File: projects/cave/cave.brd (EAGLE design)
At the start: 160 x 100 mm, 115 parts, among them U1 IRLML6344TRPBF, U10 IRLML6344TRPBF, U11 IRLML6344TRPBF, U12 IRLML6344TRPBF, U2 TLC555CDR, U3 IRLML6344TRPBF, U4 IRLML6344TRPBF, U5 IRLML6344TRPBF, U6 IRLML6344TRPBF, U7 TPS54625, U9 IRLML6344TRPBF

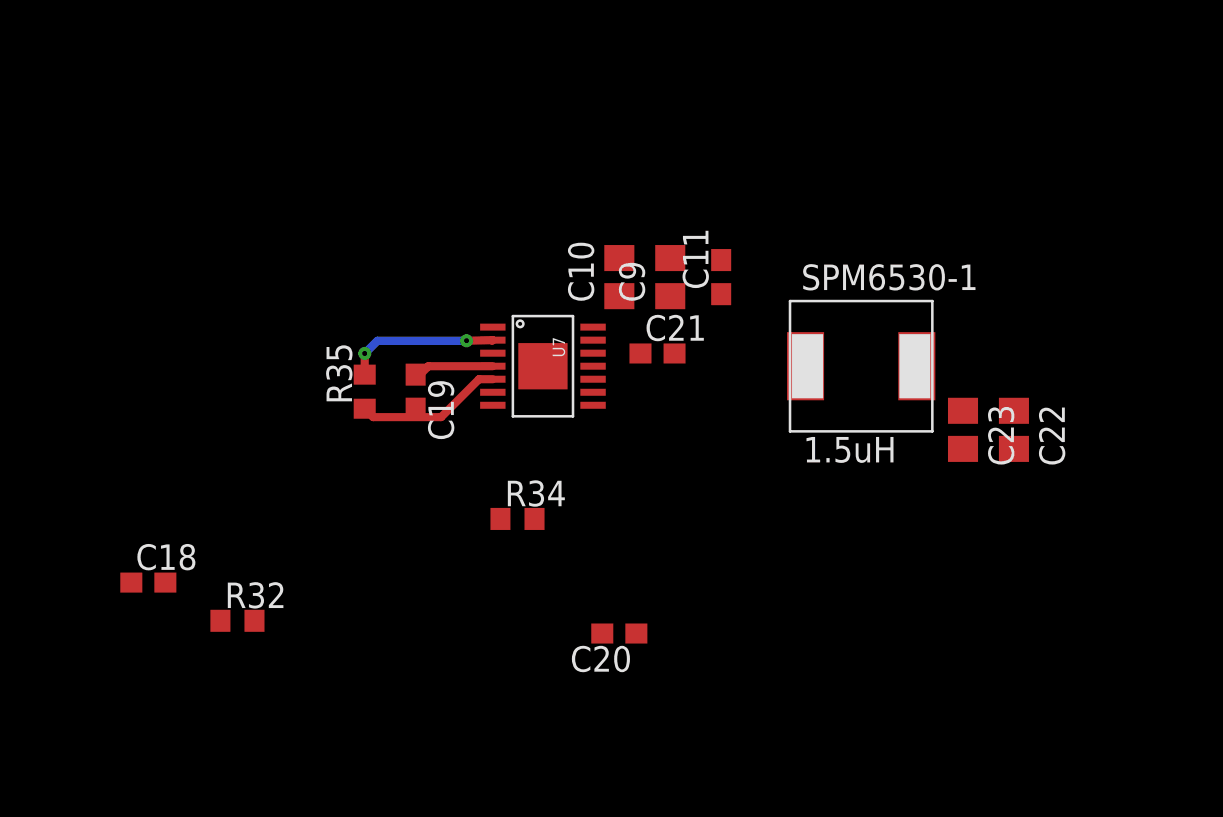
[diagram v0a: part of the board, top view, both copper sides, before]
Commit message: 5V step down regulator routed
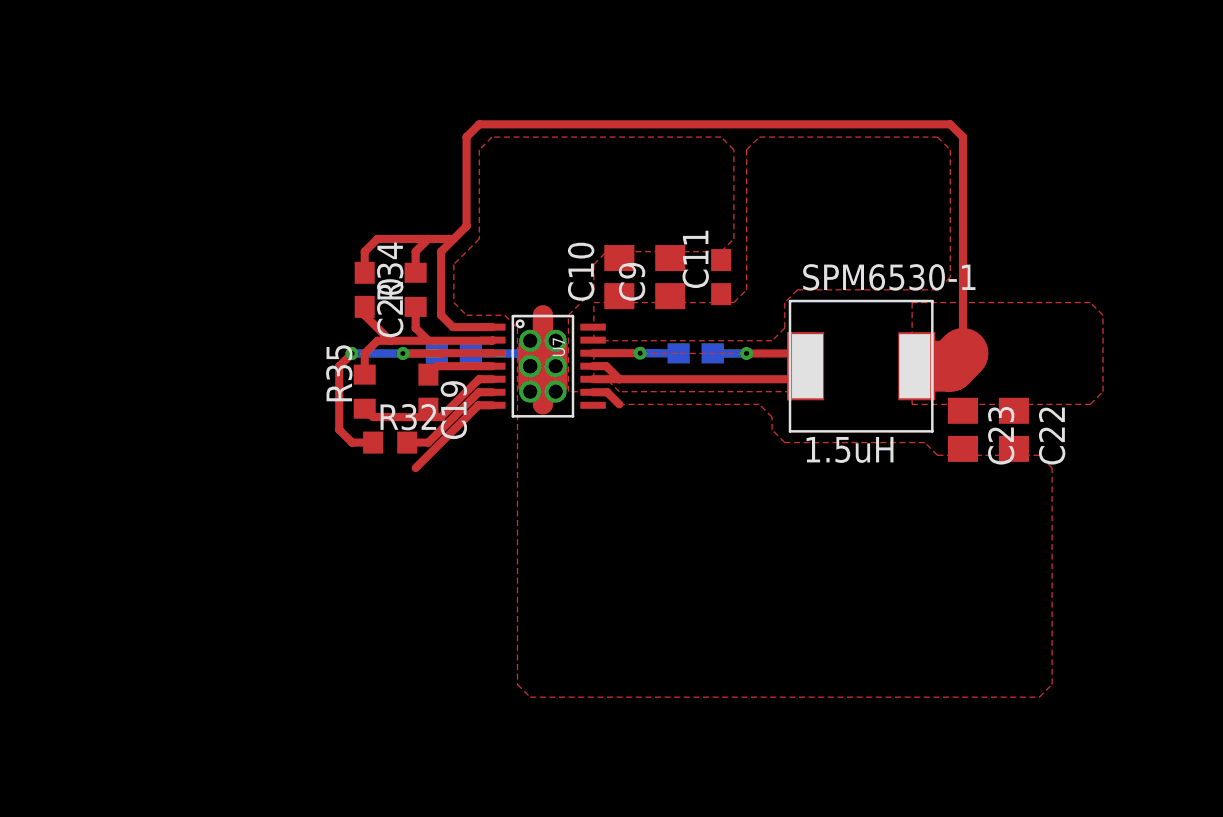
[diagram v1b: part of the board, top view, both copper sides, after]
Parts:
- moved C20 21.3 mm to (92.1, 33.7), turned to 270 degrees
- moved C18 19.0 mm to (96.5, 30.5), flipped to the bottom, turned to 180 degrees
- moved R34 12.5 mm to (94.6, 33.7), turned to 90 degrees
- moved R32 11.7 mm to (93.3, 26.0)
- moved C21 1.90 mm to (108.6, 30.5), flipped to the bottom, turned to 180 degrees
- moved C19 0.64 mm to (95.2, 28.6)
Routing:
- net +5V: track 0.00 -> 58.2 mm
- net N$36: track 0.00 -> 16.0 mm, vias 0 -> 1
- net N$28: track 0.00 -> 14.7 mm, vias 0 -> 2
- net GND: track 7.35 -> 17.8 mm, vias 0 -> 1
- net N$30: track 0.00 -> 5.31 mm
- net ENABLE: track 0.00 -> 5.15 mm
- net N$35: track 0.00 -> 4.27 mm, vias 0 -> 1
- net N$34: track 7.75 -> 11.9 mm, vias 2 -> 0
- net N$31: track 4.02 -> 3.39 mm
- net VCOND: track 0.00 -> 0.59 mm
- added copper zone on layer 1, net +5V
- added copper zone on layer 1, net GND
- added copper zone on layer 1, net N$36
- added copper zone on layer 1, net VCOND

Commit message: finished routing 5V step down regulator
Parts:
- X2: device con-subd:F09H -> con-subd:F09V
- moved C3 295.5 mm to (101.0, 19.1), turned to 90 degrees
- moved SMW5-2 246.8 mm to (39.4, 26.0)
- moved C2 246.4 mm to (78.1, 14.0), turned to 270 degrees
- moved SMW5-1 245.3 mm to (39.4, 34.3)
- moved C12 198.2 mm to (55.2, 19.1), turned to 90 degrees
- moved R2 104.3 mm to (27.3, 24.8), turned to 90 degrees
- moved D3 94.4 mm to (39.4, 40.6), turned to 270 degrees
- moved R3 85.4 mm to (27.3, 20.3), turned to 90 degrees
- moved T3 82.1 mm to (93.3, 33.7)
- moved R19 82.0 mm to (85.1, 33.0)
- moved R17 80.4 mm to (104.1, 34.3)
- moved U2 78.8 mm to (89.5, 40.0)
- moved D1 61.9 mm to (27.3, 30.5), turned to 270 degrees
- moved D2 36.6 mm to (52.1, 30.5), turned to 270 degrees
- moved D4 29.9 mm to (36.8, 15.9)
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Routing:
- net GND: track 17.8 -> 66.9 mm, vias 1 -> 2
- net VCOND: track 0.59 -> 12.7 mm
- net +5V: track 58.2 -> 66.8 mm
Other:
- board size 160 x 100 mm -> 227.3 x 162.7 mm

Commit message: 555 components placed but not routed. Updated 555 pin description in package.
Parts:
- moved R18 232.5 mm to (110.5, 3.81)
- moved T1 210.7 mm to (111.1, 6.99), turned to 90 degrees
- moved R7 210.3 mm to (123.2, 10.8), turned to 90 degrees
- moved C6 209.8 mm to (122.6, 6.99), turned to 270 degrees
- moved R8 209.5 mm to (114.6, 6.35), turned to 90 degrees
- moved C5 203.3 mm to (125.7, 6.35), turned to 270 degrees
- moved R6 203.3 mm to (123.2, 14.0), turned to 90 degrees
- moved T2 131.8 mm to (105.7, 4.76), turned to 180 degrees
- moved POWER- 119.0 mm to (3.17, 14.6)
- moved POWER+ 103.9 mm to (3.17, 21.0)
- moved D4 89.0 mm to (125.7, 10.8)
- moved U2 40.4 mm to (117.5, 10.8)
- moved R19 35.3 mm to (111.8, 9.84), turned to 180 degrees
- moved T3 27.1 mm to (108.0, 10.8), turned to 90 degrees
- moved R17 24.8 mm to (120.0, 15.2), turned to 270 degrees
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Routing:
- net VCOND: track 12.7 -> 148.1 mm, vias 0 -> 2
- net POWER_STATE: track 0.00 -> 35.2 mm, vias 0 -> 1
- net +12V: track 0.00 -> 28.3 mm
- net GND: track 66.9 -> 39.6 mm, vias 2 -> 1
- net N$3: track 0.00 -> 22.9 mm
- net N$2: track 0.00 -> 22.9 mm
- net N$4: track 0.00 -> 15.5 mm
- net N$6: track 0.00 -> 13.4 mm, vias 0 -> 2
- net N$1: track 0.00 -> 11.7 mm
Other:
- board size 227.3 x 162.7 mm -> 160 x 100 mm

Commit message: wip on routing
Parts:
- moved R3 7.73 mm to (15.9, 12.7)
- moved POWER+ 7.73 mm to (10.8, 19.7)
- moved POWER- 7.73 mm to (10.8, 13.3)
- moved R2 7.73 mm to (15.9, 17.1)
- moved T1 7.38 mm to (108.0, 13.7)
- moved R17 6.97 mm to (126.0, 18.7)
- moved D1 6.48 mm to (19.7, 18.4)
- moved T3 6.43 mm to (111.4, 16.2), turned to 0 degrees
- moved R18 4.80 mm to (111.1, 8.57)
- moved D2 4.55 mm to (38.1, 27.0), turned to 0 degrees
- moved T2 4.44 mm to (105.7, 9.21)
- moved D3 4.42 mm to (29.5, 28.3)
- moved SMW5-1 4.24 mm to (29.5, 22.5)
- moved SMW5-2 4.24 mm to (29.5, 14.3)
- moved R8 2.93 mm to (114.0, 9.21)
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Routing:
- net +12V: track 28.3 -> 122.7 mm
- net GND: track 39.6 -> 57.5 mm
- net ENABLE: track 5.15 -> 21.5 mm
- net VCOND: track 148.1 -> 163.1 mm, vias 2 -> 4
- net N$1: track 11.7 -> 22.3 mm
- net N$12: track 0.00 -> 9.90 mm
- net N$5: track 0.00 -> 9.33 mm
- net N$6: track 13.4 -> 21.9 mm
- net N$11: track 0.00 -> 7.39 mm
- net WATCHDOG: track 0.00 -> 6.09 mm
- net POWER_STATE: track 35.2 -> 39.9 mm
- net N$4: track 15.5 -> 11.5 mm
- net N$16: track 0.00 -> 3.47 mm
- net N$9: track 0.00 -> 2.66 mm
- net N$17: track 0.00 -> 2.25 mm

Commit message: "power" layout makeover in progress
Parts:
- moved X2 318.3 mm to (95.2, 60.6)
- moved X3 310.4 mm to (104.8, 27.0), turned to 90 degrees
- moved C21 109.7 mm to (28.3, 41.9)
- moved C22 109.7 mm to (44.1, 38.1)
- moved C23 109.7 mm to (41.6, 38.1)
- moved R34 109.7 mm to (14.3, 45.1)
- moved C10 109.7 mm to (24.4, 45.7)
- moved C18 109.7 mm to (16.2, 41.9)
- moved C19 109.7 mm to (14.9, 40.0)
- moved C20 109.7 mm to (11.7, 45.1)
- moved C9 109.7 mm to (27.0, 45.7)
- moved R17 109.7 mm to (17.8, 36.5)
- moved R32 109.7 mm to (13.0, 37.5)
- moved R35 109.7 mm to (11.7, 40.0)
- moved SPM6530-1 109.7 mm to (36.5, 41.3)
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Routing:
- net VCOND: track 163.1 -> 249.8 mm
- net +12V: track 122.7 -> 178.2 mm
- net ENABLE: track 21.5 -> 64.4 mm
- net POWER_STATE: track 39.9 -> 12.5 mm
- net GND: track 57.5 -> 83.2 mm
- net N$6: track 21.9 -> 15.8 mm
- net N$1: track 22.3 -> 25.5 mm

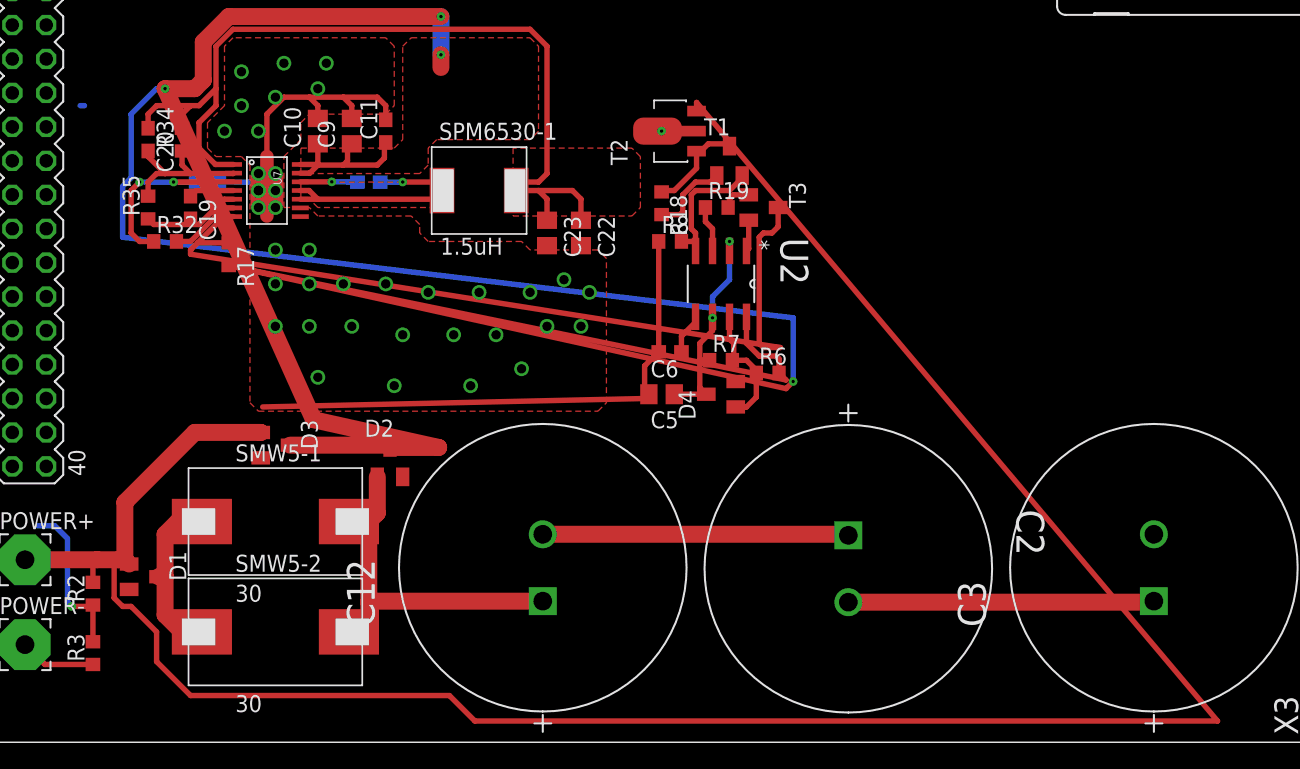
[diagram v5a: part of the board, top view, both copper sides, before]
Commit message: trying to tidy up the power sector of the board
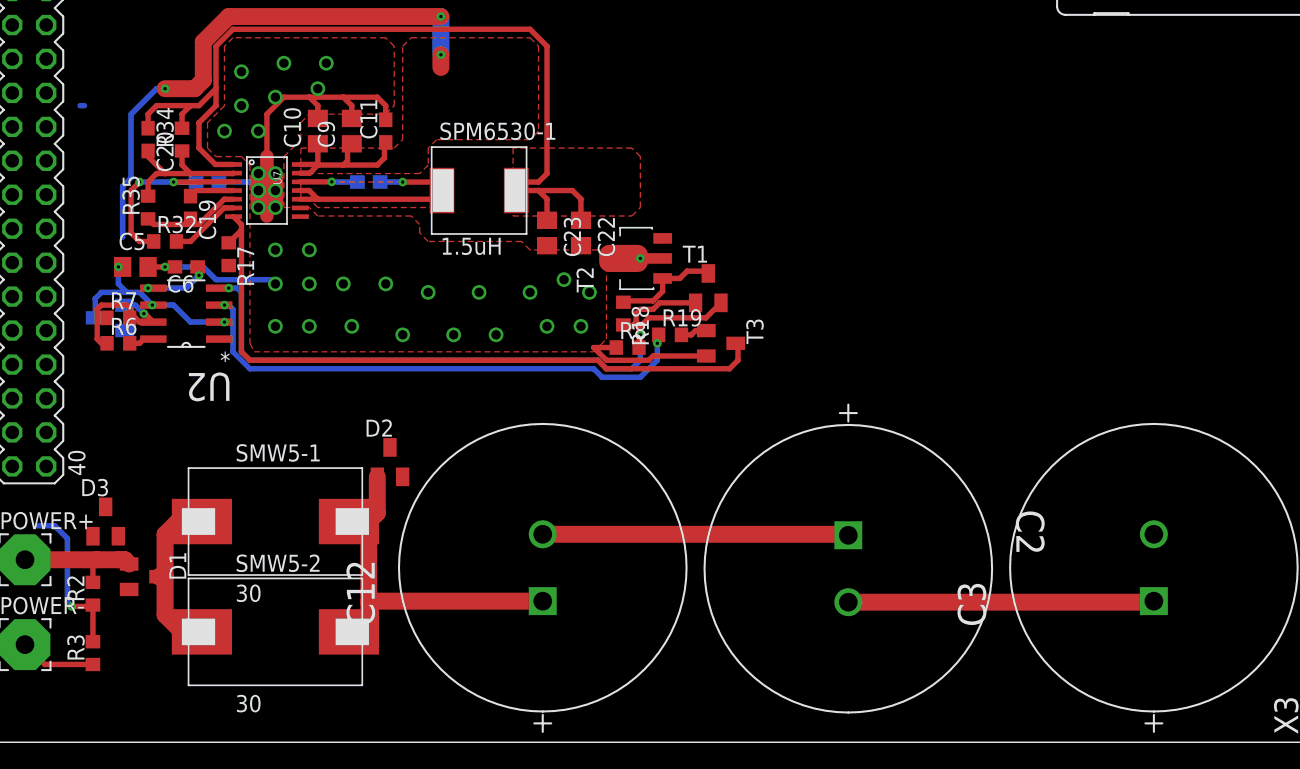
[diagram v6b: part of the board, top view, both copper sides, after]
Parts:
- moved R6 48.6 mm to (9.53, 29.8)
- moved D4 46.1 mm to (8.89, 31.8), flipped to the bottom, turned to 270 degrees
- moved R7 45.2 mm to (9.53, 31.8)
- moved C5 40.5 mm to (10.8, 35.6), turned to 0 degrees
- moved U2 40.1 mm to (14.6, 32.1), turned to 180 degrees
- moved C6 36.7 mm to (14.6, 35.6)
- moved D3 13.9 mm to (8.57, 16.5), turned to 0 degrees
- moved T3 10.6 mm to (54.6, 29.8)
- moved R19 10.1 mm to (50.8, 30.5)
- moved T2 9.86 mm to (48.3, 36.2)
- moved T1 9.66 mm to (53.7, 34.0)
- moved R18 8.74 mm to (47.3, 32.1)
- moved R8 8.55 mm to (47.6, 29.5)
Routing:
- net VCOND: track 249.8 -> 55.9 mm, vias 4 -> 3
- net +12V: track 178.2 -> 10.2 mm
- net N$12: track 9.90 -> 48.2 mm, vias 0 -> 2
- net N$16: track 3.47 -> 39.3 mm, vias 0 -> 2
- net GND: track 83.2 -> 60.9 mm, vias 1 -> 2
- net ENABLE: track 64.4 -> 51.0 mm
- net N$9: track 2.66 -> 5.28 mm, vias 0 -> 2
- net N$5: track 9.33 -> 11.1 mm, vias 0 -> 1
- net N$6: track 15.8 -> 15.2 mm, vias 2 -> 3
- net N$11: track 7.39 -> 7.95 mm

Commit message: HEAT sector routed, but not linked to the rest of the board.
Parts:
- moved HEAT_SWITCH+ 231.8 mm to (121.3, 87.6)
- moved U4 222.0 mm to (129.2, 83.2), turned to 90 degrees
- moved HEAT_SWITCH_GND 221.6 mm to (127.6, 87.6)
- moved C7 214.6 mm to (125.4, 76.8)
- moved R27 211.5 mm to (125.1, 74.6)
- moved H-5V 174.9 mm to (122.6, 82.9), turned to 90 degrees
- moved R24 161.6 mm to (129.5, 76.5), turned to 180 degrees
- moved R26 148.0 mm to (125.1, 79.7), turned to 270 degrees
- moved H-12V 145.7 mm to (120.0, 82.9), turned to 90 degrees
- moved R25 145.1 mm to (128.6, 79.1), turned to 180 degrees
- moved U5 108.5 mm to (126.0, 83.2)
- moved C1 105.6 mm to (45.7, 83.8)
- moved R42 79.9 mm to (24.8, 89.2)
- moved U12 65.3 mm to (22.5, 80.3)
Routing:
- net N$21: track 0.00 -> 16.4 mm
- net HEAT_SWITCH: track 0.00 -> 11.4 mm
- net HEAT_LEVER_F: track 0.00 -> 10.6 mm
- net GND: track 60.9 -> 71.4 mm, vias 2 -> 4
- net N$26: track 0.00 -> 8.68 mm
- net HEAT_LED: track 0.00 -> 3.93 mm
- net HEAT_LEVER_IN: track 0.00 -> 1.99 mm

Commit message: "switches" sector routed but not linked to the rest of the board.
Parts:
- moved U11 228.9 mm to (113.7, 83.2), turned to 90 degrees
- moved R43 208.7 mm to (109.5, 74.6)
- moved C8 193.4 mm to (94.0, 77.2)
- moved R31 189.9 mm to (97.2, 75.6), turned to 90 degrees
- moved DEHUM_SWITCH_GND 188.3 mm to (112.1, 87.6)
- moved R40 171.4 mm to (114.0, 76.5), turned to 180 degrees
- moved DEHUM_SWITCH+ 168.0 mm to (105.7, 87.6)
- moved R41 161.3 mm to (113.0, 79.1), turned to 180 degrees
- moved D-5V 153.0 mm to (107.0, 83.2), turned to 90 degrees
- moved F-5V 151.2 mm to (90.2, 83.2), turned to 90 degrees
- moved FAN_SWITCH_GND 140.7 mm to (94.9, 87.6)
- moved U6 137.4 mm to (94.9, 83.5), turned to 90 degrees
- moved R28 134.2 mm to (97.2, 79.7), turned to 270 degrees
- moved R30 129.3 mm to (93.7, 74.9)
- moved FAN_SWITCH+ 128.7 mm to (88.9, 87.6)
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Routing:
- net GND: track 71.4 -> 91.9 mm, vias 4 -> 7
- net N$24: track 0.00 -> 17.9 mm
- net DEHUM_SWITCH: track 0.00 -> 11.4 mm
- net FAN_SWITCH: track 0.00 -> 11.2 mm
- net DEHUM_LEVER_F: track 0.00 -> 10.5 mm
- net FAN_LEVER_F: track 0.00 -> 9.90 mm
- net N$23: track 0.00 -> 9.04 mm
- net N$27: track 0.00 -> 8.04 mm
- net N$22: track 0.00 -> 8.04 mm
- net FAN_LED: track 0.00 -> 7.35 mm
- net FAN_LEVER_IN: track 0.00 -> 4.53 mm
- net DEHUM_LED: track 0.00 -> 3.93 mm
- net DEHUM_LEVER_IN: track 0.00 -> 1.99 mm
